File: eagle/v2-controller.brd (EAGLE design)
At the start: 66 x 40.6 mm, 16 parts, among them Q1 DHT##, Q2 RS485-ADAPTER0.05-CONNECTOR, X1 RJ45-6L21-B

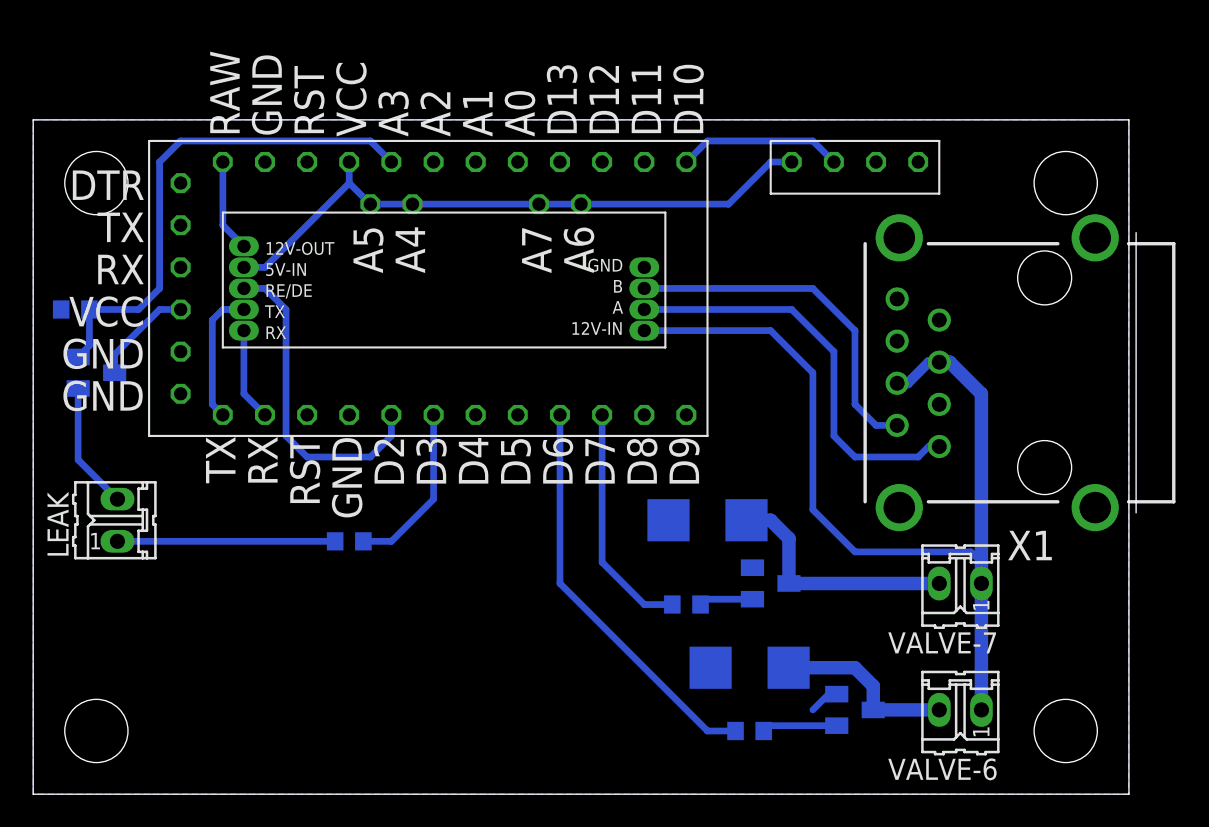
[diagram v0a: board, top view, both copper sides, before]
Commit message: Moving v2 sprinkler board controls to the same location. Adding a buzzed for alerting when water leak is detected.
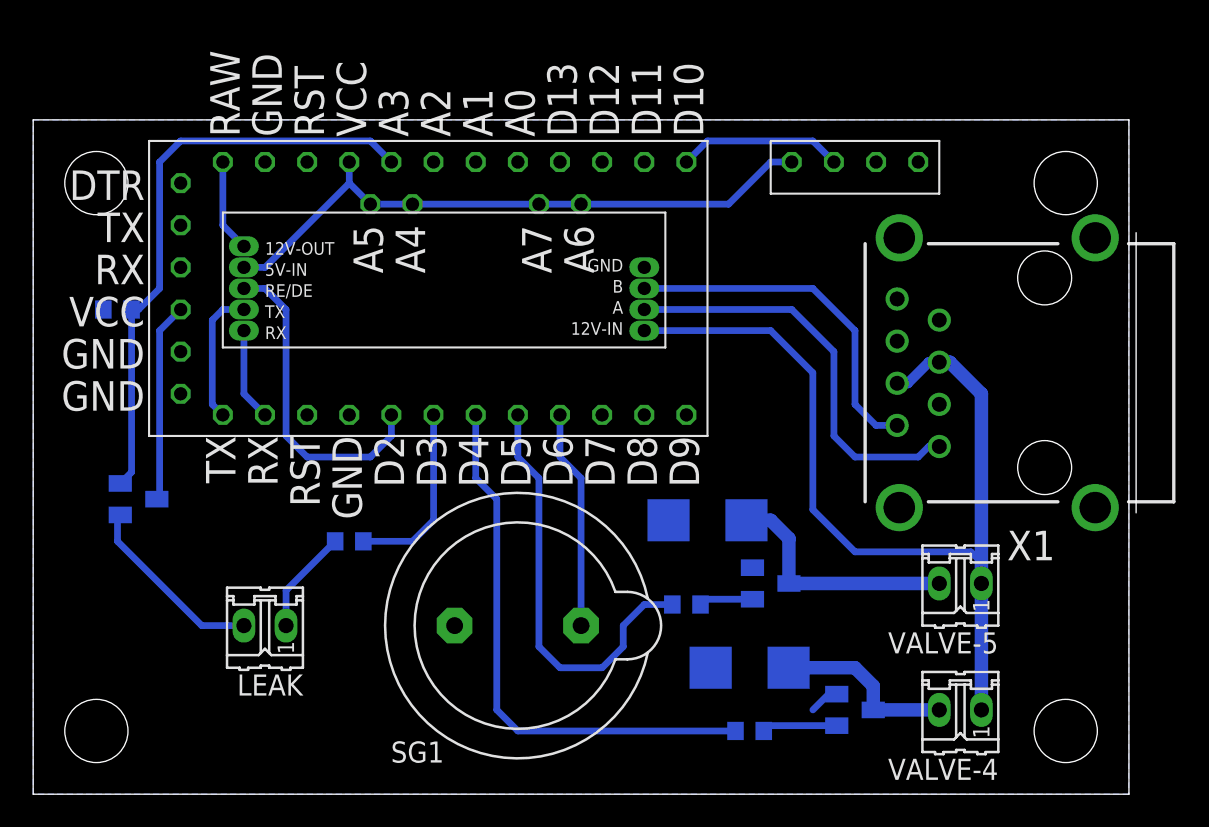
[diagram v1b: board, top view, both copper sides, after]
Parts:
- added SG1: F/HGP, buzzer:F/HGP
- moved LEAK 10.9 mm to (14.0, 10.2), turned to 180 degrees
- moved T3 8.03 mm to (6.35, 17.8)
- moved R4 2.54 mm to (5.08, 29.2)
- renumbered VALVE-6 to VALVE-4, VALVE-7 to VALVE-5
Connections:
- net D4: now also R1.1
- net D5: now also R2.1
- net D6: now also SG1.1; no longer R1.1
- net D7: no longer R2.1
- net GND: now also SG1.2
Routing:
- net D4: track 0.00 -> 33.2 mm
- net D5: track 0.00 -> 25.4 mm
- net D7: track 14.2 -> 0.00 mm
- net D6: track 24.4 -> 13.2 mm
- net N$1: track 13.1 -> 6.31 mm
- net VCC: track 44.2 -> 50.0 mm
- net A3: track 30.5 -> 35.6 mm
- net N$3: track 7.65 -> 11.4 mm
- net D3: track 10.4 -> 11.1 mm

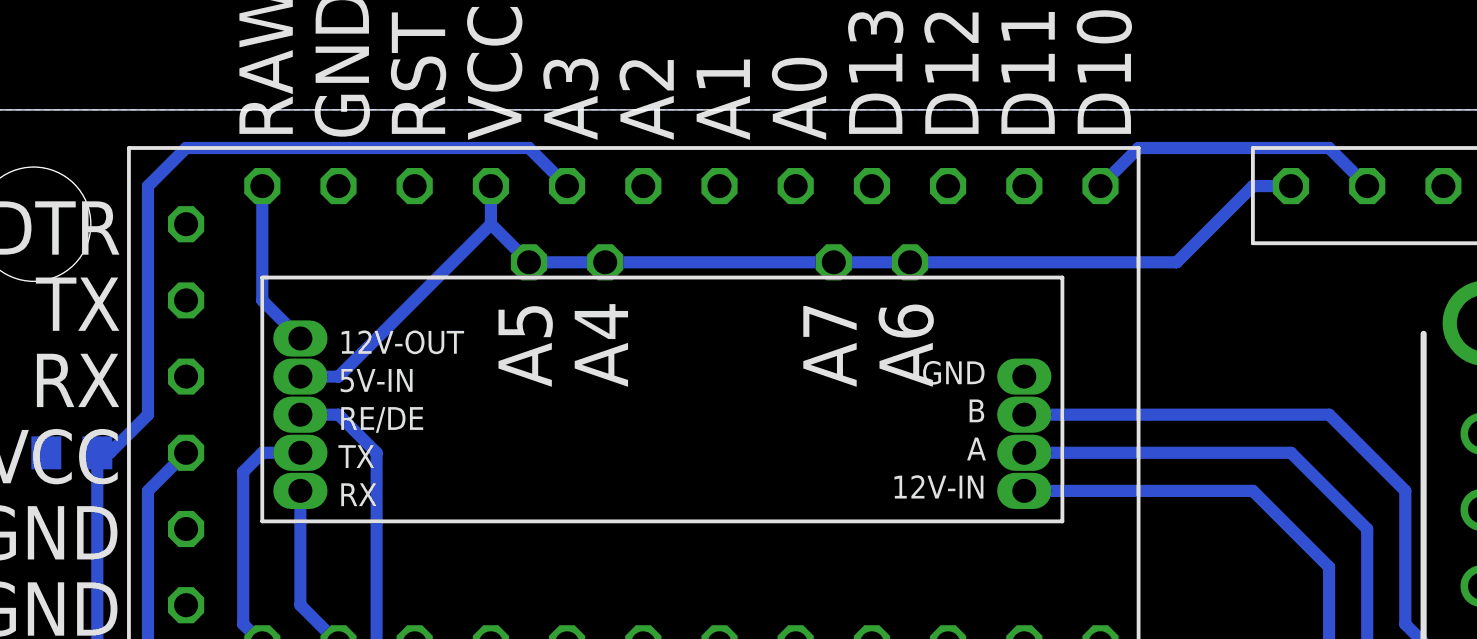
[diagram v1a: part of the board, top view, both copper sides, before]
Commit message: Fixed going over analog pins for one of the traces.
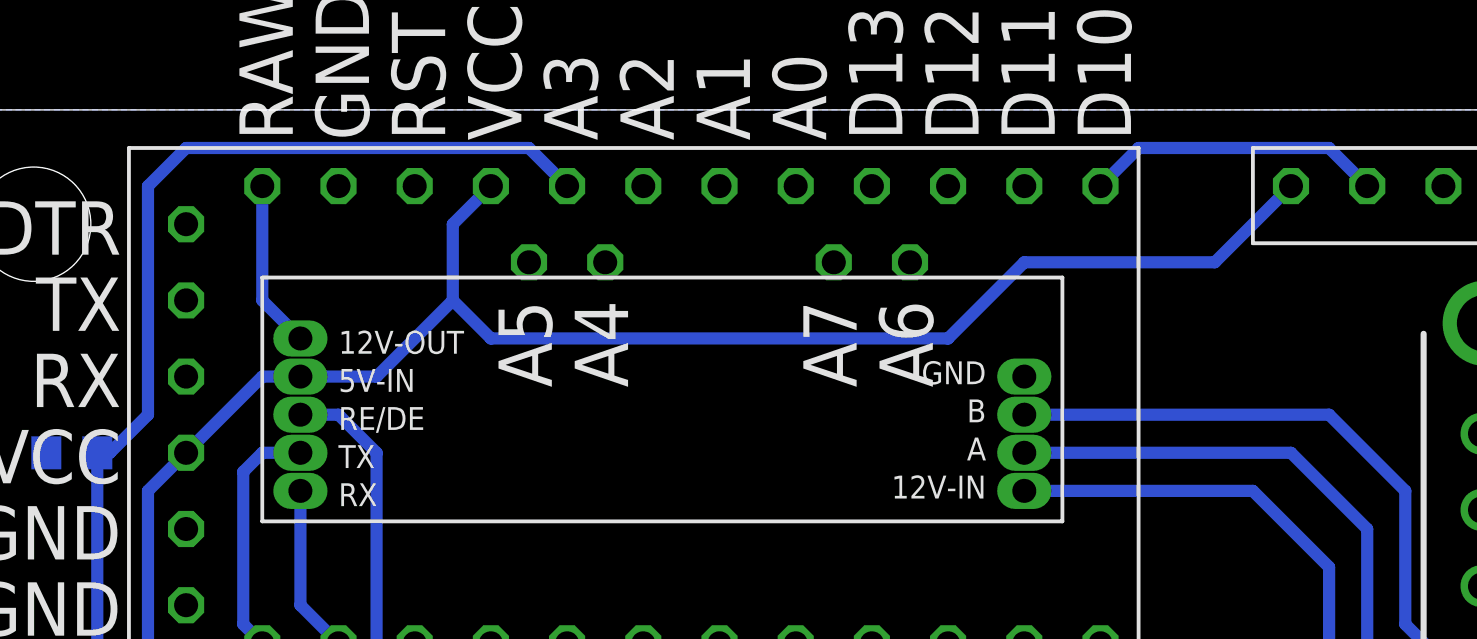
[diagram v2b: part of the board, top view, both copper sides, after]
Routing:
- net VCC: track 50.0 -> 57.9 mm
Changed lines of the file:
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@@
 <contactref element="Q1" pad="VCC"/>
 <contactref element="Q1" pad="VCC"/>
-<wire x1="19.05" y1="38.1" x2="19.05" y2="36.83" width="0.4064" layer="16"/>
-<wire x1="19.05" y1="36.83" x2="13.97" y2="31.75" width="0.4064" layer="16"/>
-<wire x1="45.72" y1="38.1" x2="44.45" y2="38.1" width="0.4064" layer="16"/>
-<wire x1="44.45" y1="38.1" x2="41.91" y2="35.56" width="0.4064" layer="16"/>
-<wire x1="41.91" y1="35.56" x2="20.32" y2="35.56" width="0.4064" layer="16"/>
-<wire x1="20.32" y1="35.56" x2="19.05" y2="36.83" width="0.4064" layer="16"/>
 <contactref element="Q2" pad="5V-IN"/>
-<wire x1="12.7" y1="31.75" x2="13.97" y2="31.75" width="0.4064" layer="16"/>
 <contactref element="U$1" pad="VCC1"/>
 <contactref element="U$1" pad="VCC2"/>
@@
 <wire x1="7.62" y1="27.94" x2="7.62" y2="17.95" width="0.4064" layer="16"/>
 <wire x1="7.62" y1="17.95" x2="7.45" y2="17.78" width="0.4064" layer="16"/>
-<wire x1="8.89" y1="29.21" x2="12.7" y2="31.75" width="0" layer="19" extent="1-1"/>
+<wire x1="45.72" y1="38.1" x2="43.18" y2="35.56" width="0.4064" layer="16"/>
+<wire x1="43.18" y1="35.56" x2="36.83" y2="35.56" width="0.4064" layer="16"/>
+<wire x1="36.83" y1="35.56" x2="34.29" y2="33.02" width="0.4064" layer="16"/>
+<wire x1="34.29" y1="33.02" x2="19.05" y2="33.02" width="0.4064" layer="16"/>
+<wire x1="19.05" y1="33.02" x2="17.78" y2="34.29" width="0.4064" layer="16"/>
+<wire x1="17.78" y1="34.29" x2="17.78" y2="36.83" width="0.4064" layer="16"/>
+<wire x1="17.78" y1="36.83" x2="19.05" y2="38.1" width="0.4064" layer="16"/>
+<wire x1="12.7" y1="31.75" x2="15.24" y2="31.75" width="0.4064" layer="16"/>
+<wire x1="15.24" y1="31.75" x2="17.78" y2="34.29" width="0.4064" layer="16"/>
+<wire x1="8.89" y1="29.21" x2="11.43" y2="31.75" width="0.4064" layer="16"/>
+<wire x1="11.43" y1="31.75" x2="12.7" y2="31.75" width="0.4064" layer="16"/>
 </signal>
 <signal name="N$7">
